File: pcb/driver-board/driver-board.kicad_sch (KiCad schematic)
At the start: 116 parts, among them Q1 IRLML6344, Q10 IRLML6344, Q11 IRLML6344, Q12 2N7002, Q2 IRLML6344, Q3 IRLML6344, Q4 IRLML6344, Q5 IRLML6344, Q6 IRLML6344, Q7 IRLML6344, Q8 IRLML6344, Q9 IRLML6344, U1 MP1584EN_12V, U2 MP1584EN_6V5, U3 MP1584EN_5V, U4 DRV8876, U5 DRV8876, U6 TB6612FNG, U7 INA219, U8 PCF8574

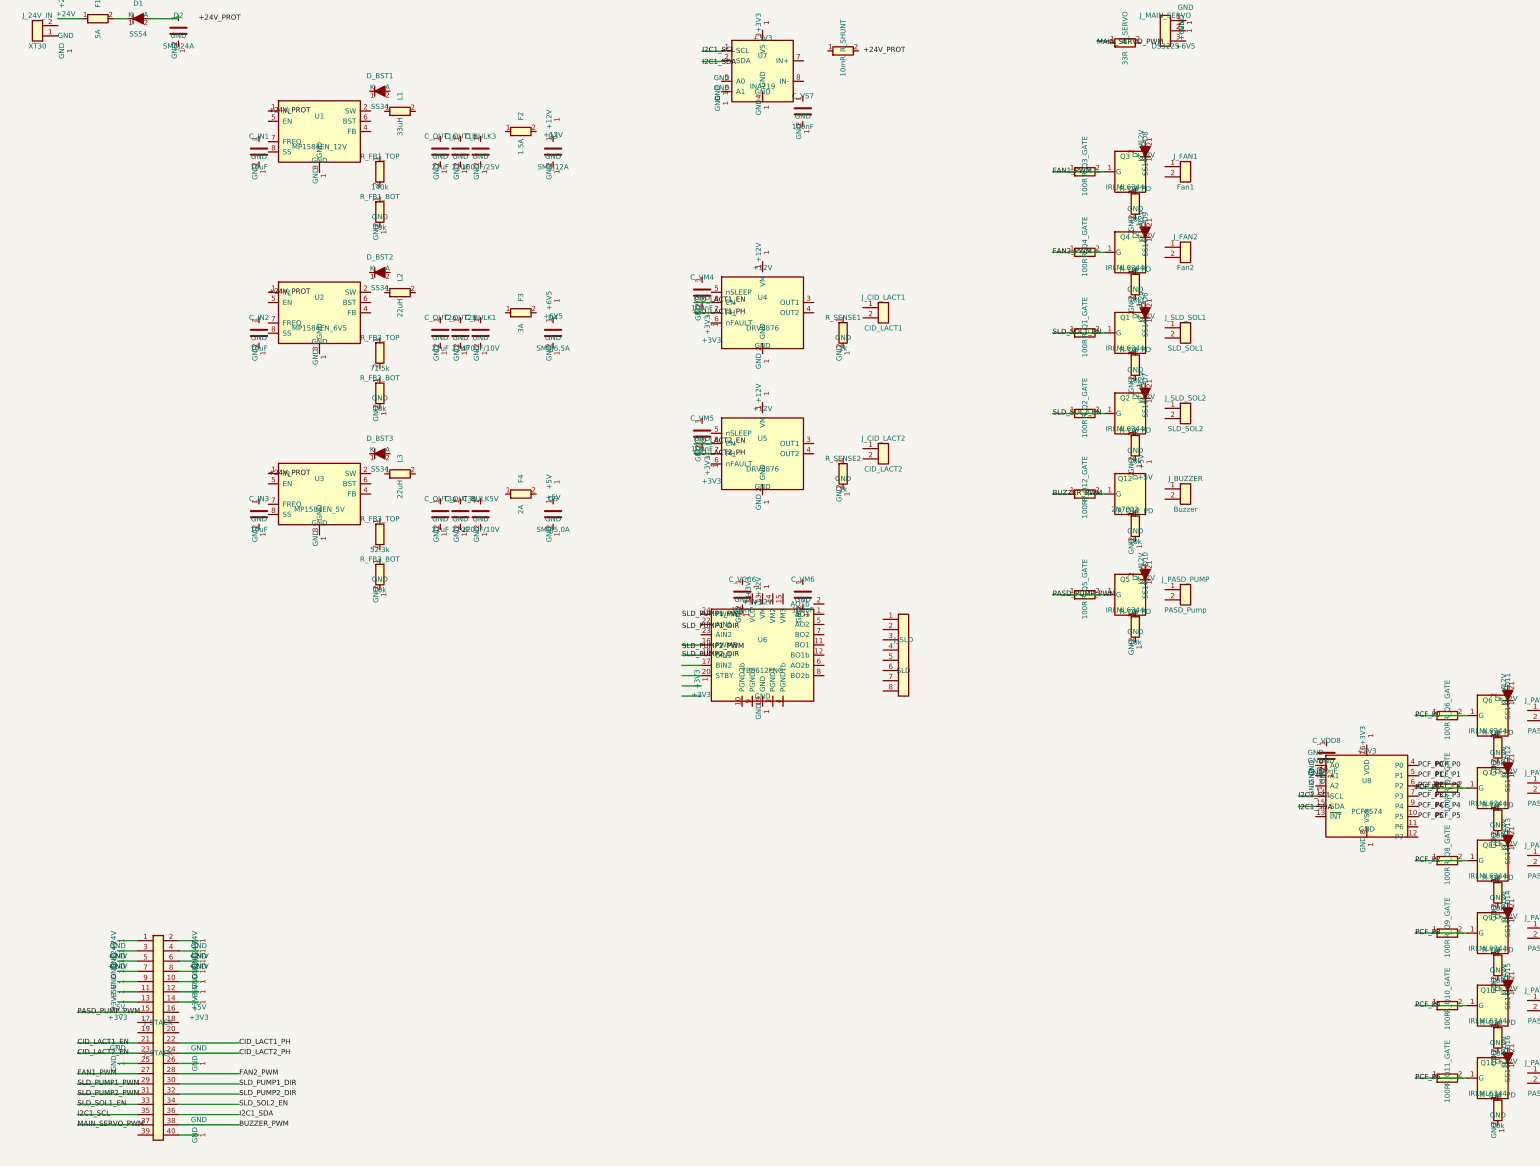
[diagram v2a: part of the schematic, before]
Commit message: Add UX epic, JSX mock app, Live Activity/Glance stories, and OTP auth endpoints
- New UX epic (13 epics total) with 8 stories for mobile screen mocks
- Vite+React mock app in mocks/ with Liquid Glass aesthetic: login, OTP,
  recipe grid, favourites, sessions, profile, mini progress
- Tab bar updated from Home/Recipes/Cook/Profile to Recipe/Favourite/Session/Profile
  across IOS, AND epics and Mobile Architecture docs
- Phone+OTP auth endpoints (POST /auth/otp/request, /auth/otp/verify) added to REST API
- IOS-LIVE.01 (ActivityKit Live Activity) and AND-LIVE.01 (Jetpack Glance widget) stories
- Updated GitHub Project epic field IDs in CLAUDE.md after UX option addition
- Driver board schematic updates

Co-Authored-By: Claude Opus 4.6 <noreply@anthropic.com>
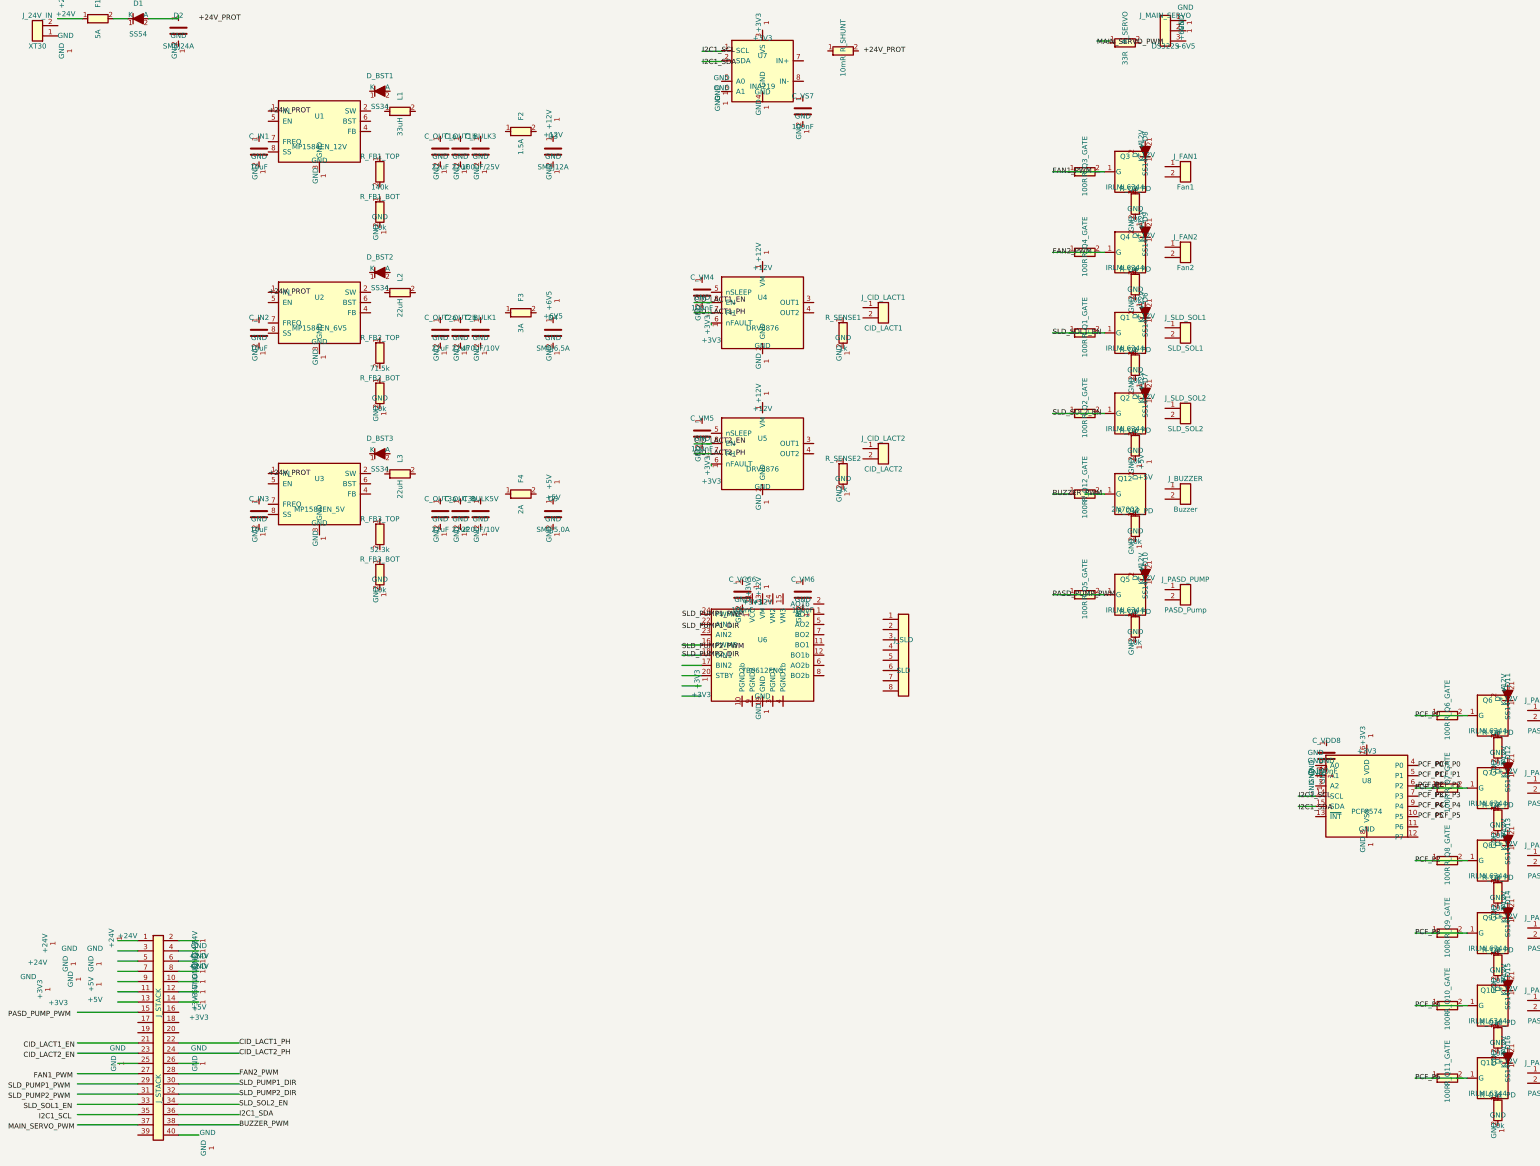
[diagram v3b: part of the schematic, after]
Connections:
- net CID_LACT1_EN: no longer J_STACK.21 (Pin_21)
- net CID_LACT2_EN: no longer J_STACK.23 (Pin_23)
- net FAN1_PWM: no longer J_STACK.27 (Pin_27)
- net I2C1_SCL: no longer J_STACK.35 (Pin_35)
- net MAIN_SERVO_PWM: no longer J_STACK.37 (Pin_37)
- net PASD_PUMP_PWM: no longer J_STACK.15 (Pin_15)
- net SLD_PUMP1_PWM: no longer J_STACK.29 (Pin_29)
- net SLD_PUMP2_PWM: no longer J_STACK.31 (Pin_31)
- net SLD_SOL1_EN: no longer J_STACK.33 (Pin_33)
